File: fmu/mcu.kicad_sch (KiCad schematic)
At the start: 20 parts, among them IC1 nRF52840-QFAA-F-R7, IC2 EFR32FG28B320F1024IM68-AR

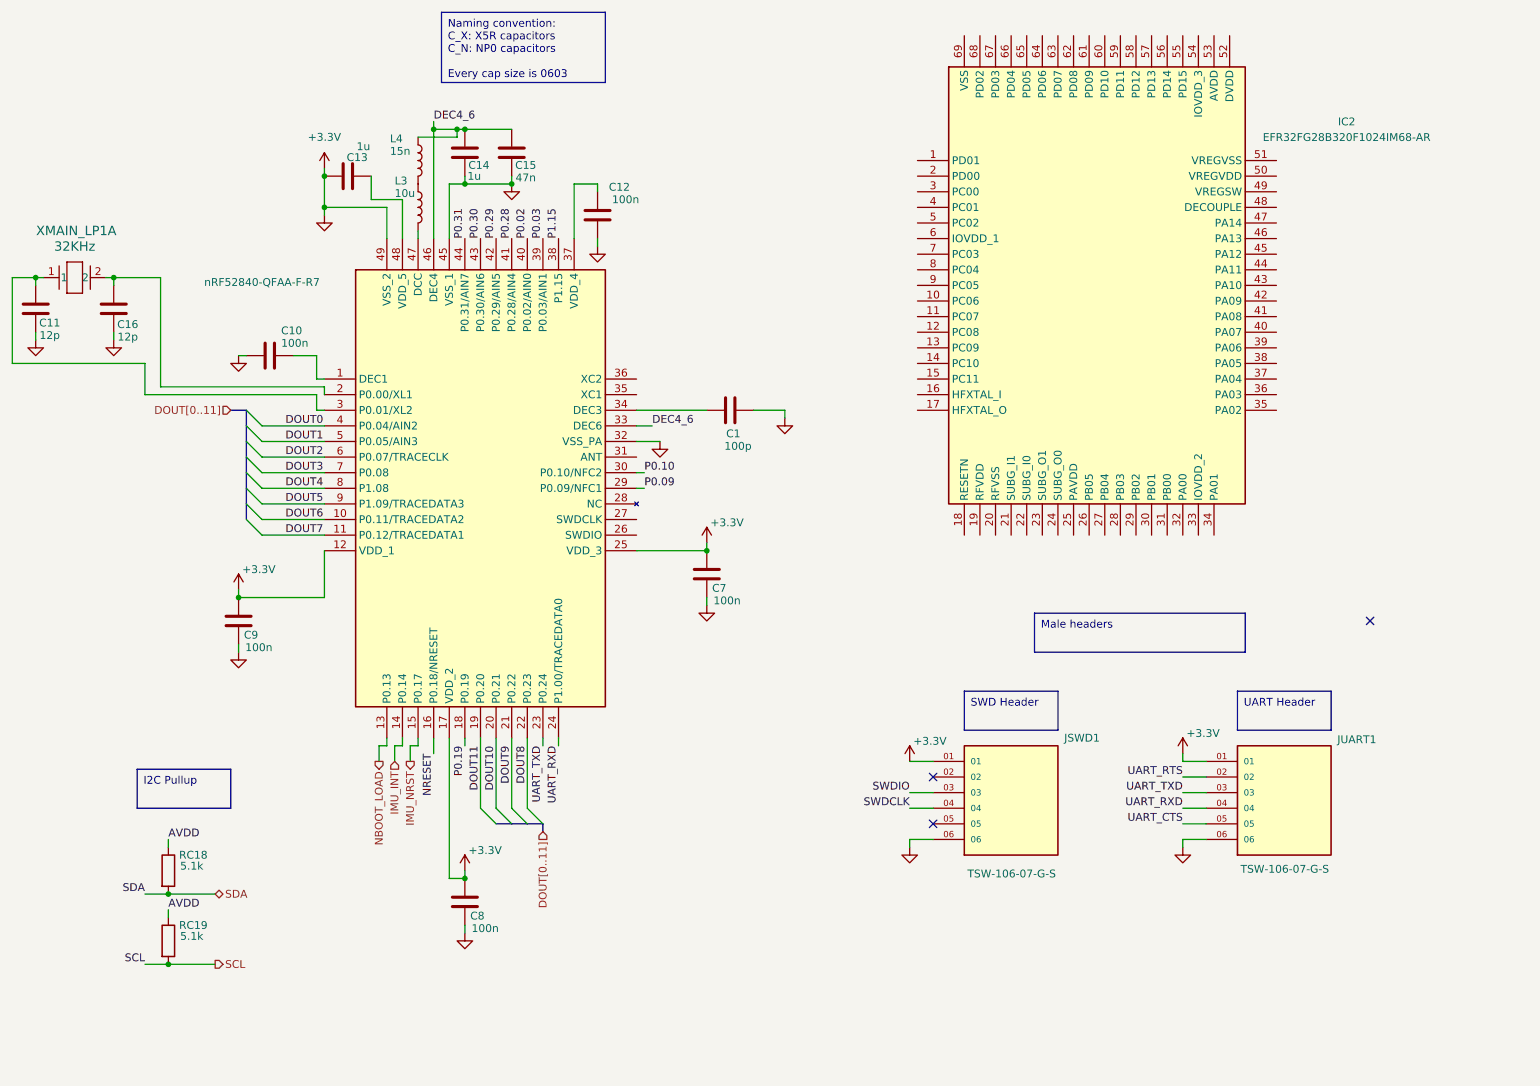
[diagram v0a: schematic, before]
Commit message: Replace nRF52840 with EFR32FG28
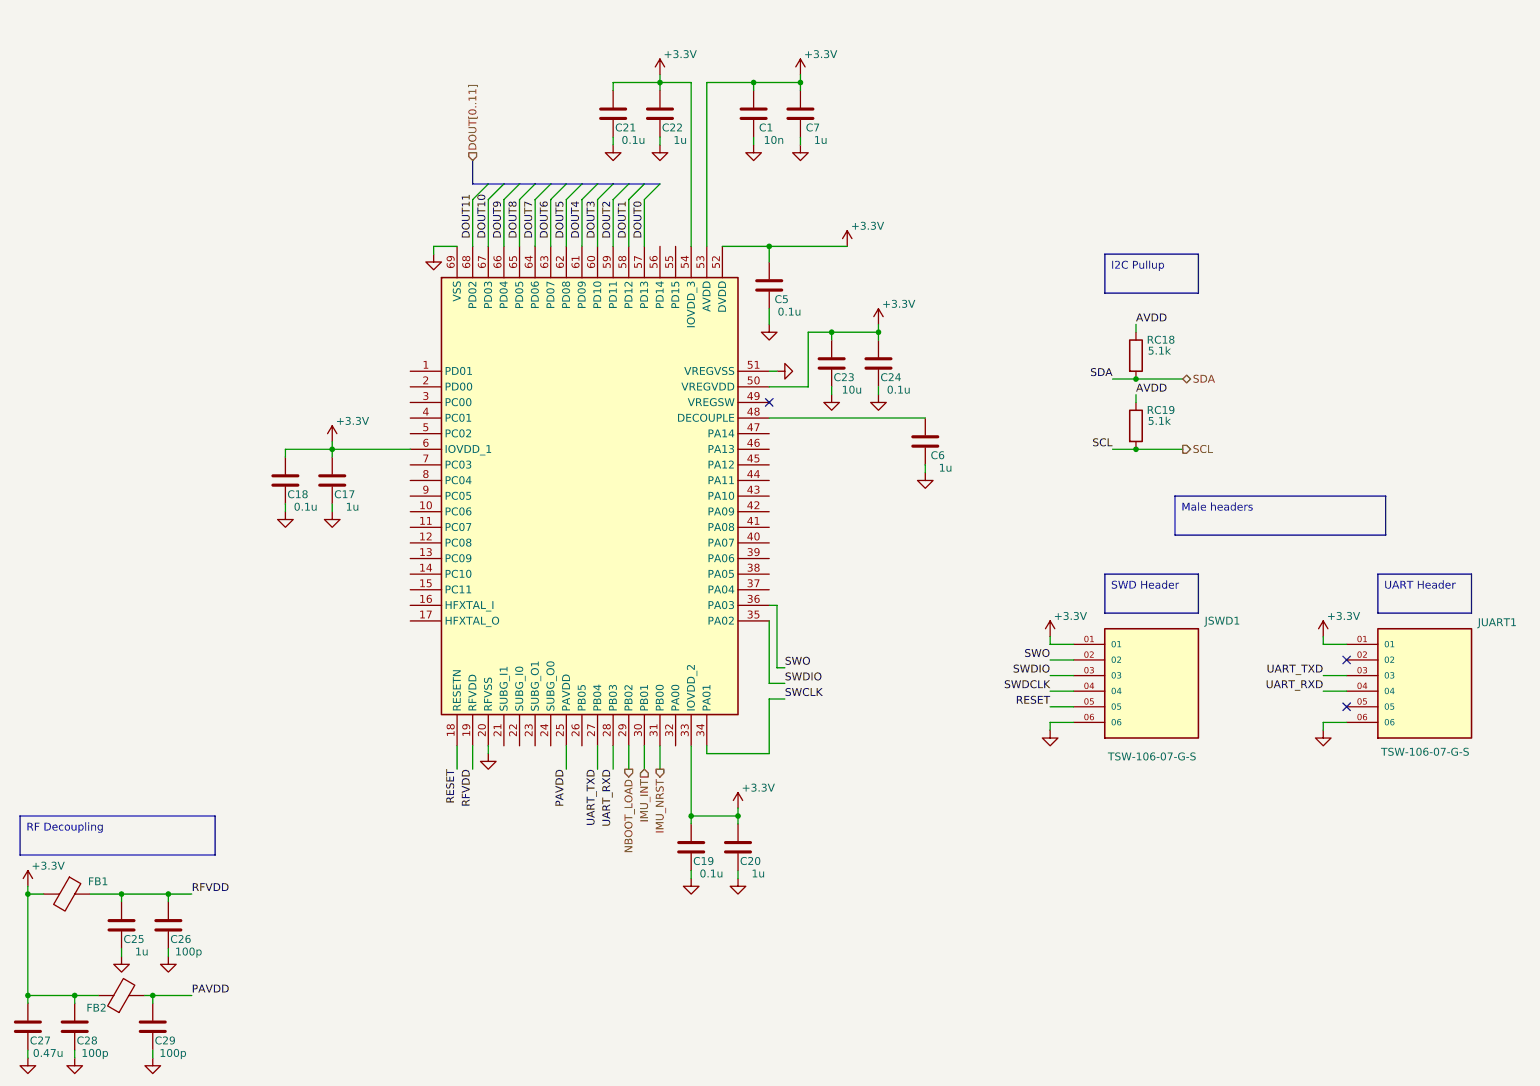
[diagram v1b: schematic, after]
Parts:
- removed C10, C12, C8, C9: 100n, Capacitor_SMD:C_0603_1608Metric, symbol Device:C
- removed C11, C16: 12p, Capacitor_SMD:C_0603_1608Metric, symbol Device:C
- removed C13, C14: 1u, Capacitor_SMD:C_0603_1608Metric, symbol Device:C
- removed C15: 47n, Capacitor_SMD:C_0603_1608Metric, symbol Device:C
- removed IC1: nRF52840-QFAA-F-R7, QFN40P600X600X95-49N-D, symbol nRF52840-QFAA-F-R7:nRF52840-QFAA-F-R7
- removed L3: 10u, Inductor_SMD:L_0603_1608Metric, symbol Device:L
- removed L4: 15n, Inductor_SMD:L_0603_1608Metric, symbol Device:L
- removed XMAIN_LP1: 32KHz, XTAL_ABS07-32.768KHZ-7-T_ABR, symbol 2024-04-14_16-25-50:ABS07-32.768KHZ-7-T
- added C17, C20, C22, C25, C6: 1u, Capacitor_SMD:C_0603_1608Metric, symbol Device:C
- added C18, C19, C21, C24, C5: 0.1u, Capacitor_SMD:C_0603_1608Metric, symbol Device:C
- added C23: 10u, Capacitor_SMD:C_0603_1608Metric, symbol Device:C
- added C26, C28, C29: 100p, Capacitor_SMD:C_0603_1608Metric, symbol Device:C
- added C27: 0.47u, Capacitor_SMD:C_0603_1608Metric, symbol Device:C
- added FB1: 2512067007Y3, Inductor_SMD:L_1206_3216Metric, symbol Device:FerriteBead
- added FB2: BLM31PG330SN1L, Inductor_SMD:L_1206_3216Metric, symbol Device:FerriteBead
- C1: value 100p -> 10n; Type NP0 -> X5R
- C7: value 100n -> 1u
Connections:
- net +3.3V: now also IC2.33 (IOVDD_2), IC2.50 (VREGVDD), IC2.52 (DVDD), IC2.53 (AVDD), IC2.54 (IOVDD_3), IC2.6 (IOVDD_1), C17.2, C18.2, C19.2, C20.2, C21.2, C22.2, C23.2, C24.2, C27.2, C28.2, C5.2, FB1.2, FB2.1; no longer C7.1, JSWD1.06, JUART1.06
- net DOUT0: now also IC2.57 (PD13)
- net DOUT1: now also IC2.58 (PD12)
- net DOUT10: now also IC2.67 (PD03)
- net DOUT11: now also IC2.68 (PD02)
- net DOUT2: now also IC2.59 (PD11)
- net DOUT3: now also IC2.60 (PD10)
- net DOUT4: now also IC2.61 (PD09)
- net DOUT5: now also IC2.62 (PD08)
- net DOUT6: now also IC2.63 (PD07)
- net DOUT7: now also IC2.64 (PD06)
- net DOUT8: now also IC2.65 (PD05)
- net DOUT9: now also IC2.66 (PD04)
- net IMU_INT: now also IC2.30 (PB01)
- net IMU_NRST: now also IC2.31 (PB00)
- net NBOOT_LOAD: now also IC2.29 (PB02)
- net SWDIO: now also IC2.35 (PA02)
- net UART_RXD: now also IC2.28 (PB03)
- net UART_TXD: now also IC2.27 (PB04)
- net GND: now reaches C1.1
- net GND: now also C7.1, IC2.20 (RFVSS), IC2.51 (VREGVSS), IC2.69 (VSS), JSWD1.06, JUART1.06, C17.1, C18.1, C19.1, C20.1, C21.1, C22.1, C23.1, C24.1, C25.1, C26.1, C27.1, C28.1, C29.1, C5.1, C6.1
- net SWO: now reaches JSWD1.02
- net SWO: now also IC2.36 (PA03)
- net RESET: now reaches JSWD1.05
- net RESET: now also IC2.18 (RESETN)
- net RFVDD: now reaches IC2.19 (RFVDD)
- net RFVDD: now also C25.2, C26.2, FB1.1
- net PAVDD: now reaches IC2.25 (PAVDD)
- net PAVDD: now also C29.2, FB2.2
- net SWCLK: now reaches IC2.34 (PA01)
- net at IC2.48 (DECOUPLE): now also C6.2
- net UART_CTS: no longer names the net of JUART1.05
- net UART_RTS: no longer names the net of JUART1.02
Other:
- moved on the sheet: JSWD1, JUART1

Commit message: Connect motors and MCU
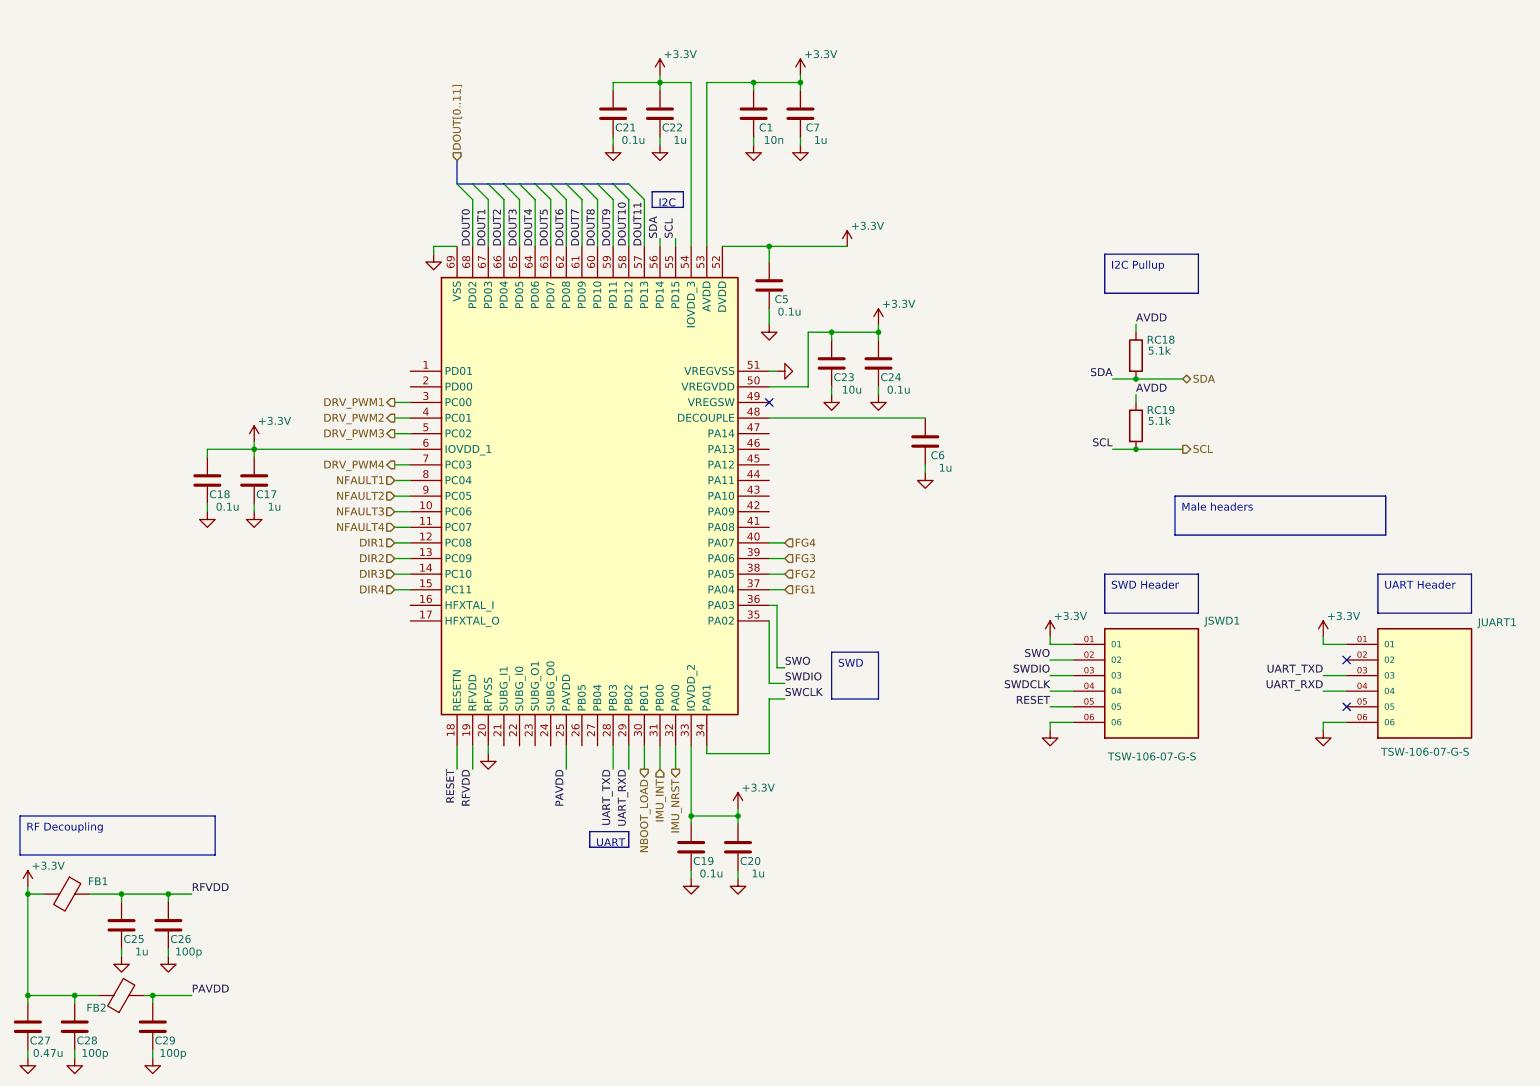
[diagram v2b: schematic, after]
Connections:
- net DOUT0: now also IC2.68 (PD02); no longer IC2.57 (PD13)
- net DOUT1: now also IC2.67 (PD03); no longer IC2.58 (PD12)
- net DOUT10: now also IC2.58 (PD12); no longer IC2.67 (PD03)
- net DOUT11: now also IC2.57 (PD13); no longer IC2.68 (PD02)
- net DOUT2: now also IC2.66 (PD04); no longer IC2.59 (PD11)
- net DOUT3: now also IC2.65 (PD05); no longer IC2.60 (PD10)
- net DOUT4: now also IC2.64 (PD06); no longer IC2.61 (PD09)
- net DOUT5: now also IC2.63 (PD07); no longer IC2.62 (PD08)
- net DOUT6: now also IC2.62 (PD08); no longer IC2.63 (PD07)
- net DOUT7: now also IC2.61 (PD09); no longer IC2.64 (PD06)
- net DOUT8: now also IC2.60 (PD10); no longer IC2.65 (PD05)
- net DOUT9: now also IC2.59 (PD11); no longer IC2.66 (PD04)
- net IMU_INT: now also IC2.31 (PB00); no longer IC2.30 (PB01)
- net IMU_NRST: now also IC2.32 (PA00); no longer IC2.31 (PB00)
- net NBOOT_LOAD: now also IC2.30 (PB01); no longer IC2.29 (PB02)
- net SCL: now also IC2.55 (PD15)
- net SDA: now also IC2.56 (PD14)
- net UART_RXD: now also IC2.29 (PB02); no longer IC2.28 (PB03)
- net UART_TXD: now also IC2.28 (PB03); no longer IC2.27 (PB04)
- net NFAULT3: now reaches IC2.10 (PC06)
- net NFAULT4: now reaches IC2.11 (PC07)
- net DIR1: now reaches IC2.12 (PC08)
- net DIR2: now reaches IC2.13 (PC09)
- net DIR3: now reaches IC2.14 (PC10)
- net DIR4: now reaches IC2.15 (PC11)
- net DRV_PWM1: now reaches IC2.3 (PC00)
- net FG1: now reaches IC2.37 (PA04)
- net FG2: now reaches IC2.38 (PA05)
- net FG3: now reaches IC2.39 (PA06)
- net DRV_PWM2: now reaches IC2.4 (PC01)
- net FG4: now reaches IC2.40 (PA07)
- net DRV_PWM3: now reaches IC2.5 (PC02)
- net DRV_PWM4: now reaches IC2.7 (PC03)
- net NFAULT1: now reaches IC2.8 (PC04)
- net NFAULT2: now reaches IC2.9 (PC05)
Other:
- moved on the sheet: C17, C18

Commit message: Add voltage regulators
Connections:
- net PIXCLK: now reaches IC2.45 (PA12)
- net FRAME_VALID: now reaches IC2.46 (PA13)
- net LINE_VALID: now reaches IC2.47 (PA14)
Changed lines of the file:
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@@
+	(wire
+		(pts
+			(xy 147.32 83.82) (xy 149.86 83.82)
+		)
+		(stroke
+			(width 0)
+			(type default)
+		)
+	)
 	(wire
 		(pts
@@
 	(wire
 		(pts
+			(xy 147.32 88.9) (xy 149.86 88.9)
+		)
+		(stroke
+			(width 0)
+			(type default)
+		)
+	)
+	(wire
+		(pts
 			(xy 104.14 45.72) (xy 104.14 53.34)
 		)
@@
 		(pts
 			(xy 142.24 146.05) (xy 142.24 147.32)
+		)
+		(stroke
+			(width 0)
+			(type default)
+		)
+	)
+	(wire
+		(pts
+			(xy 147.32 86.36) (xy 149.86 86.36)
 		)
 		(stroke
@@
 	(label "DOUT3"
 		(at 106.68 53.34 90)
+		(fields_autoplaced yes)
 		(effects
 			(font
@@
 	(label "DOUT5"
 		(at 111.76 53.34 90)
+		(fields_autoplaced yes)
 		(effects
 			(font
@@
 	(label "DOUT10"
 		(at 124.46 53.34 90)
+		(fields_autoplaced yes)
 		(effects
 			(font
@@
 	(label "DOUT4"
 		(at 109.22 53.34 90)
+		(fields_autoplaced yes)
 		(effects
 			(font
@@
 	(label "DOUT11"
 		(at 127 53.34 90)
+		(fields_autoplaced yes)
 		(effects
 			(font
@@
 	(label "DOUT2"
 		(at 104.14 53.34 90)
+		(fields_autoplaced yes)
 		(effects
 			(font
@@
 	(label "DOUT7"
 		(at 116.84 53.34 90)
+		(fields_autoplaced yes)
 		(effects
 			(font
@@
 	(label "DOUT6"
 		(at 114.3 53.34 90)
+		(fields_autoplaced yes)
 		(effects
 			(font
@@
 	(label "DOUT1"
 		(at 101.6 53.34 90)
+		(fields_autoplaced yes)
 		(effects
 			(font
@@
 	(label "DOUT0"
 		(at 99.06 53.34 90)
+		(fields_autoplaced yes)
 		(effects
 			(font
@@
 	(label "DOUT8"
 		(at 119.38 53.34 90)
+		(fields_autoplaced yes)
 		(effects
 			(font
@@
 	(label "DOUT9"
 		(at 121.92 53.34 90)
-		(effects
-			(font
-				(size 1.27 1.27)
-			)
-			(justify left bottom)
+		(fields_autoplaced yes)
+		(effects
+			(font
+				(size 1.27 1.27)
+			)
+			(justify left bottom)
+		)
+	)
+	(hierarchical_label "LINE_VALID"
+		(shape input)
+		(at 149.86 83.82 0)
+		(fields_autoplaced yes)
+		(effects
+			(font
+				(size 1.27 1.27)
+			)
+			(justify left)
 		)
 	)
@@
 		)
 	)
+	(hierarchical_label "FRAME_VALID"
+		(shape input)
+		(at 149.86 86.36 0)
+		(fields_autoplaced yes)
+		(effects
+			(font
+				(size 1.27 1.27)
+			)
+			(justify left)
+		)
+	)
+	(hierarchical_label "PIXCLK"
+		(shape input)
+		(at 149.86 88.9 0)
+		(fields_autoplaced yes)
+		(effects
+			(font
+				(size 1.27 1.27)
+			)
+			(justify left)
+		)
+	)

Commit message: Fix some connections
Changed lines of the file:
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@@
 	(text_box "I2C"
 		(exclude_from_sim no)
-		(at 128.27 44.45 0)
-		(size 5.08 2.54)
+		(at 128.27 43.18 0)
+		(size 5.08 3.81)
 		(stroke
 			(width 0)
@@
 		(exclude_from_sim no)
 		(at 118.11 148.59 0)
-		(size 6.35 2.54)
+		(size 6.35 3.81)
 		(stroke
 			(width 0)

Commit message: Add SD Card reader
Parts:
- added C40: 2p, Capacitor_SMD:C_0603_1608Metric, symbol Device:C
- added C41: 7.6p, Capacitor_SMD:C_0603_1608Metric, symbol Device:C
- added C42: 1.3p, Capacitor_SMD:C_0603_1608Metric, symbol Device:C
- added C43: 220p, Capacitor_SMD:C_0603_1608Metric, symbol Device:C
- added L3: 1.5n, Inductor_SMD:L_0603_1608Metric, symbol Device:L
- added L4: 1.3n, Inductor_SMD:L_0603_1608Metric, symbol Device:L
- added L8: 13n, Inductor_SMD:L_0603_1608Metric, symbol Device:L
- added L9: 18n, Inductor_SMD:L_0603_1608Metric, symbol Device:L
- added Y1: ACAG1204-868-T, ANTC12040X170N, symbol ACAG1204-868-T:ACAG1204-868-T
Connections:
- net GND: now also C41.1, C42.1, Y1.2
- net SUBG_I: now reaches IC2.21 (SUBG_I1)
- net SUBG_I: now also L9.1
- net SUBG_O: now reaches IC2.23 (SUBG_O1)
- net SUBG_O: now also C40.2, L3.1
- new net: C40.1, L3.2, L4.1
- new net: C43.1, L9.2, Y1.1
- new net: C41.2, L4.2, L8.1
- new net: C42.2, C43.2, L8.2
- no-connect marks 3 -> 5
